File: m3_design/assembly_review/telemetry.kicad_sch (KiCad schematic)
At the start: 39 parts, among them J30 GNSS ANT SMA, J31 RADIO ANT SMA, Q30 AO3401A, Q31 AO3400A, Q32 S8550, U30 MAX-F10S-00B, U31 E22-900MM22S

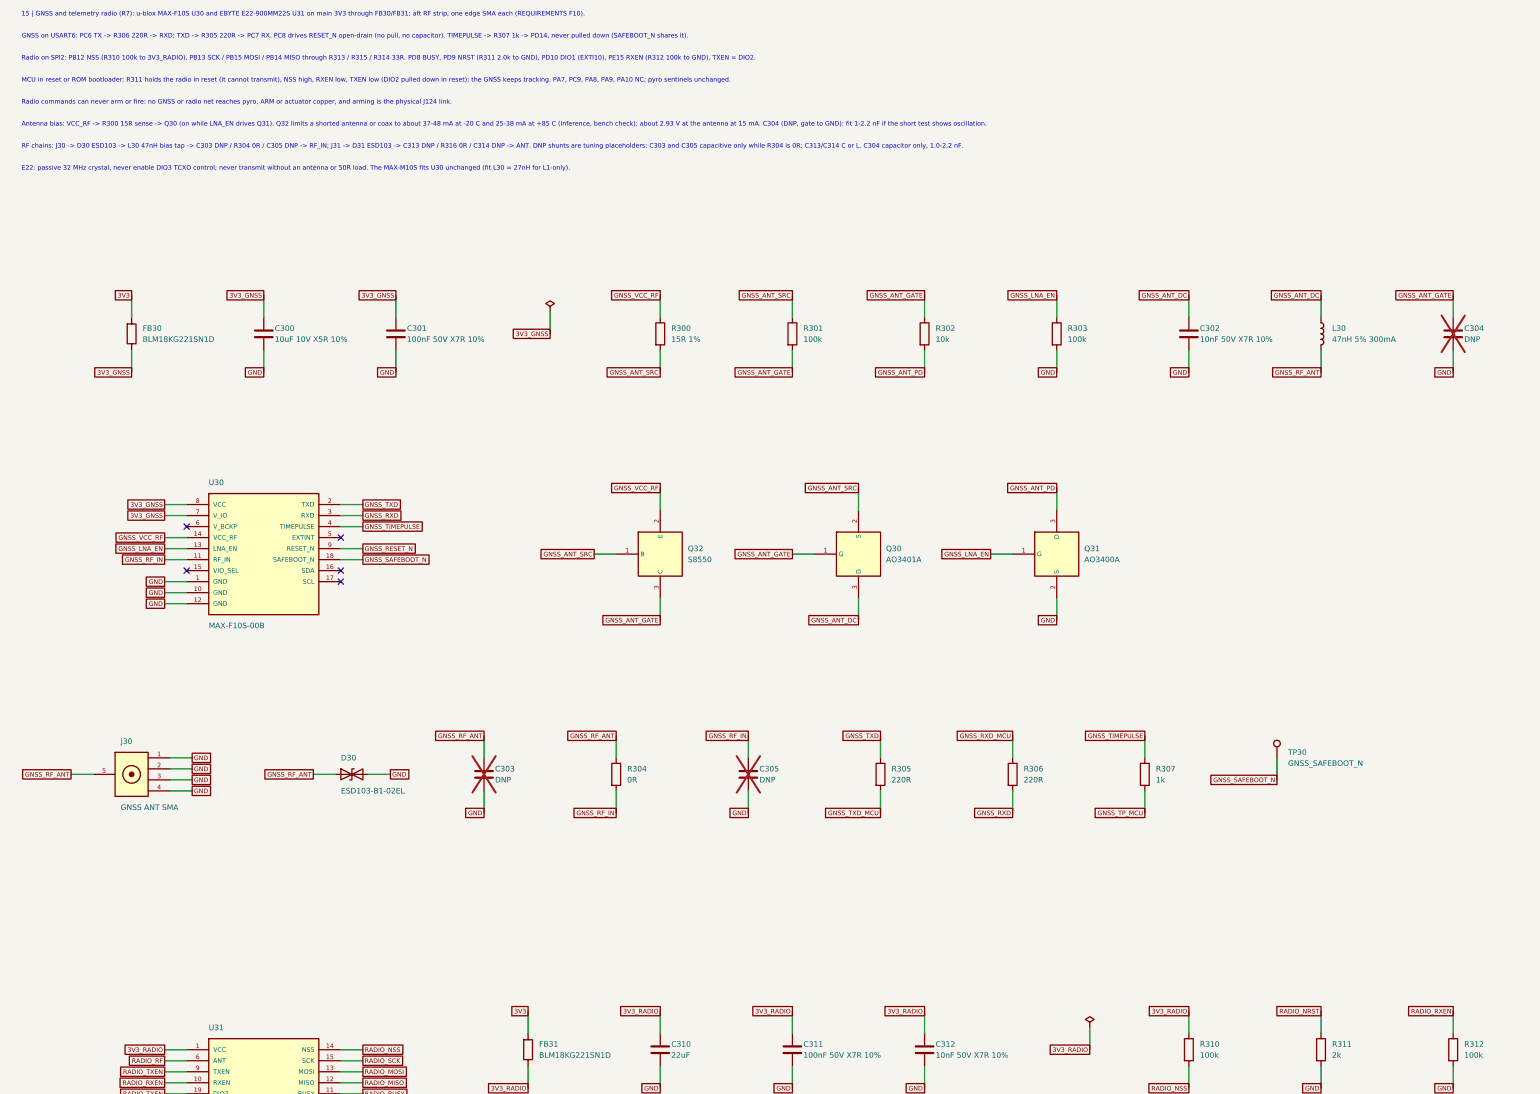
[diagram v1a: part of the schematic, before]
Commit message: M3-ASSY-R8: re-placed layout with planned-bus routing, owner-accepted deviations
R8 keeps R7's circuit, RF strip and CH1 pyro block (copied rigidly and
hash-asserted) and re-places everything else: U1 rotated so its free
pins face the RF strip, each block beside the U1 face it talks to, input
protection back at J1, and a fresh deterministic build (r8_build.sh)
with planned-bus routing, no autorouter and no patch stages.

Against R7: signal track 3.36 m -> 1.50 m, signal vias 217 -> 55,
simplicity index 100 -> 15.3, gate exceptions 74 -> 3, hard routing-rule
instances 10 -> 1, 7.7 A neck rise 38/30/44 -> 17.6/14.8/22.3 C,
unreferenced critical samples 27.9 % -> 11.1 %, non-pyro nets within
3 mm of armed copper 23 -> 7.

- Gate: check_r8 (pin contract from pin_table.tsv, F10 separation,
  battery/pyro clearance, loader-pin rule, rigid hashes), route_check
  profile r8, scorecard, dc_solve --necks, reference_audit, paste_check
- Review: passes 2, 3 and 4 found 0 Critical / 0 Major in all eight
  dimensions; pass 5 re-checked the final board (routing, planes,
  integrity) with 0 Critical / 0 Major
- Owner accepted the R8 deviation list on 2026-10-20, including the C10
  vibration item and the listed agent decisions

Board SHA-256 cc044ea0922ff826df19af9d9726d92c096ab2b127025b55d123d8772e5fb4a7.
tools/check.sh: DRC 0, unconnected 0, parity 0, ERC 0; audit, silk,
R8 contract, routing hygiene (0 failing, 3 allowlisted), actuator
contract and fit OK. Before ordering: consign U4, JLC tab acceptance,
cost/stock run within 24 h.

Co-Authored-By: Claude Opus 5.5 <noreply@anthropic.com>
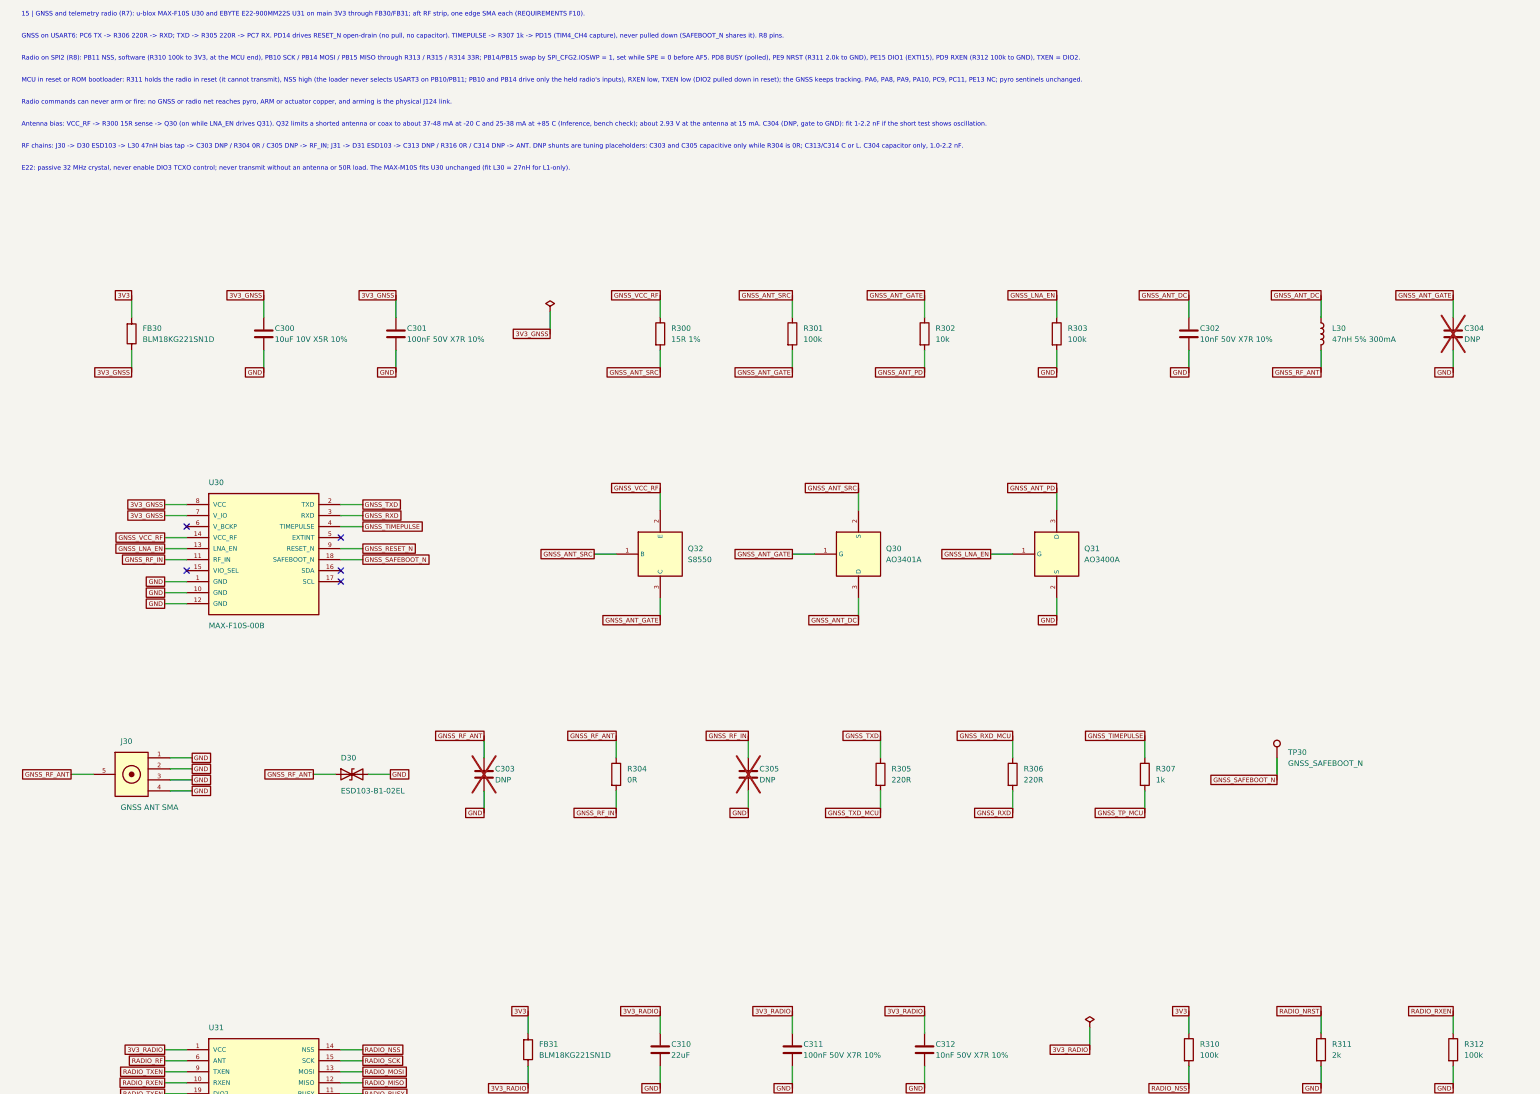
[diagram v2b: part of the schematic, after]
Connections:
- net 3V3: now also R310.1
- net 3V3_RADIO: no longer R310.1
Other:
- note added: "GNSS on USART6: PC6 TX -> R306 220R -> RXD; TXD -> R305 220R -> PC7 RX. PD14 drives RESET_N open-drain (no pull, no capacitor). TIMEPULSE -> R307 1k -> PD15 (TIM4_CH4 capture), never pulled down (SAFEBOOT_N shares it). R8 pins."
- note added: "MCU in reset or ROM bootloader: R311 holds the radio in reset (it cannot transmit), NSS high (the loader never selects USART3 on PB10/PB11; PB10 and PB14 drive only the held radio's inputs), RXEN low, TXEN low (DIO2 pulled down in reset); the GNSS keeps tracking. PA6, PA8, PA9, PA10, PC9, PC11, PE13 NC; pyro sentinels unchanged."
- note added: "Radio on SPI2 (R8): PB11 NSS, software (R310 100k to 3V3, at the MCU end), PB10 SCK / PB14 MOSI / PB15 MISO through R313 / R315 / R314 33R; PB14/PB15 swap by SPI_CFG2.IOSWP = 1, set while SPE = 0 before AF5. PD8 BUSY (polled), PE9 NRST (R311 2.0k to GND), PE15 DIO1 (EXTI15), PD9 RXEN (R312 100k to GND), TXEN = DIO2."
- note removed: "GNSS on USART6: PC6 TX -> R306 220R -> RXD; TXD -> R305 220R -> PC7 RX. PC8 drives RESET_N open-drain (no pull, no capacitor). TIMEPULSE -> R307 1k -> PD14, never pulled down (SAFEBOOT_N shares it)."
- note removed: "MCU in reset or ROM bootloader: R311 holds the radio in reset (it cannot transmit), NSS high, RXEN low, TXEN low (DIO2 pulled down in reset); the GNSS keeps tracking. PA7, PC9, PA8, PA9, PA10 NC; pyro sentinels unchanged."
- note removed: "Radio on SPI2: PB12 NSS (R310 100k to 3V3_RADIO), PB13 SCK / PB15 MOSI / PB14 MISO through R313 / R315 / R314 33R. PD8 BUSY, PD9 NRST (R311 2.0k to GND), PD10 DIO1 (EXTI10), PE15 RXEN (R312 100k to GND), TXEN = DIO2."
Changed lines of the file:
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@@
 		(title "15 | GNSS and telemetry radio (R7)")
 		(date "2026-10-15")
-		(rev "M3-ASSY-R7")
+		(rev "M3-ASSY-R8")
 		(company "Single-board M3 candidate; on-board GNSS and radio, not bench-verified"))
 	(text "15 | GNSS and telemetry radio (R7): u-blox MAX-F10S U30 and EBYTE E22-900MM22S U31 on main 3V3 through FB30/FB31; aft RF strip, one edge SMA each (REQUIREMENTS F10)."
@@
 			(justify left))
 )
-	(text "GNSS on USART6: PC6 TX -> R306 220R -> RXD; TXD -> R305 220R -> PC7 RX. PC8 drives RESET_N open-drain (no pull, no capacitor). TIMEPULSE -> R307 1k -> PD14, never pulled down (SAFEBOOT_N shares it)."
+	(text "GNSS on USART6: PC6 TX -> R306 220R -> RXD; TXD -> R305 220R -> PC7 RX. PD14 drives RESET_N open-drain (no pull, no capacitor). TIMEPULSE -> R307 1k -> PD15 (TIM4_CH4 capture), never pulled down (SAFEBOOT_N shares it). R8 pins."
 		(at 20.32 20.32 0)
 		(effects
@@
 			(justify left))
 )
-	(text "Radio on SPI2: PB12 NSS (R310 100k to 3V3_RADIO), PB13 SCK / PB15 MOSI / PB14 MISO through R313 / R315 / R314 33R. PD8 BUSY, PD9 NRST (R311 2.0k to GND), PD10 DIO1 (EXTI10), PE15 RXEN (R312 100k to GND), TXEN = DIO2."
+	(text "Radio on SPI2 (R8): PB11 NSS, software (R310 100k to 3V3, at the MCU end), PB10 SCK / PB14 MOSI / PB15 MISO through R313 / R315 / R314 33R; PB14/PB15 swap by SPI_CFG2.IOSWP = 1, set while SPE = 0 before AF5. PD8 BUSY (polled), PE9 NRST (R311 2.0k to GND), PE15 DIO1 (EXTI15), PD9 RXEN (R312 100k to GND), TXEN = DIO2."
 		(at 20.32 25.4 0)
 		(effects
@@
 			(justify left))
 )
-	(text "MCU in reset or ROM bootloader: R311 holds the radio in reset (it cannot transmit), NSS high, RXEN low, TXEN low (DIO2 pulled down in reset); the GNSS keeps tracking. PA7, PC9, PA8, PA9, PA10 NC; pyro sentinels unchanged."
+	(text "MCU in reset or ROM bootloader: R311 holds the radio in reset (it cannot transmit), NSS high (the loader never selects USART3 on PB10/PB11; PB10 and PB14 drive only the held radio's inputs), RXEN low, TXEN low (DIO2 pulled down in reset); the GNSS keeps tracking. PA6, PA8, PA9, PA10, PC9, PC11, PE13 NC; pyro sentinels unchanged."
 		(at 20.32 30.48 0)
 		(effects
@@
 			(type default))
 )
-	(global_label "3V3_RADIO"
+	(global_label "3V3"
 		(shape passive)
 		(at 289.56 245.11 0)

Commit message: R10: m3_design/r10_build.sh and per-family stage gate; m3_design/assembly_review rebuilt as M3-ASSY-R10 (board 883d2db5..., 46 x 90 mm); tools/check.sh passes at zero; binding note bound to the board
Co-Authored-By: Claude Opus 5.5 <noreply@anthropic.com>
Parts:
- removed C300: 10uF 10V X5R 10%, rocket:C0603, symbol M3:C
- removed C301, C311: 100nF 50V X7R 10%, rocket:C0402, symbol M3:C
- removed C302, C312: 10nF 50V X7R 10%, rocket:C0402, symbol M3:C
- removed C303, C304, C305, C313, C314: DNP, rocket:C0402_DNP, symbol M3:C
- removed C310: 22uF, rocket:C0805, symbol M3:C
- removed D30, D31: ESD103-B1-02EL, rocket:M3_TSLP_2_20, symbol M3:ESD_Bidir
- removed FB30, FB31: BLM18KG221SN1D, rocket:M3_BLM18K_0603, symbol M3:FerriteBead
- removed J30: GNSS ANT SMA, rocket:M3_SMA_KH_KE8_EDGE, symbol M3:SMA_Edge
- removed J31: RADIO ANT SMA, rocket:M3_SMA_KH_KE8_EDGE, symbol M3:SMA_Edge
- removed L30: 47nH 5% 300mA, rocket:M3_LQG15_0402, symbol M3:L
- removed Q30: AO3401A, rocket:SOT-23-3_L2.9-W1.3-P1.90-LS2.4-BR, symbol M3:PMOS_SOT23
- removed Q31: AO3400A, rocket:SOT-23-3_L2.9-W1.3-P1.90-LS2.4-BR, symbol M3:NMOS_SOT23
- removed Q32: S8550, rocket:SOT-23-3_L2.9-W1.3-P1.90-LS2.4-BR, symbol M3:PNP_SOT23
- removed R300: 15R 1%, rocket:R_0603_1608Metric, symbol M3:R
- removed R301, R303, R310, R312: 100k, rocket:R0402, symbol M3:R
- removed R302: 10k, rocket:R0402, symbol M3:R
- removed R304, R316: 0R, rocket:R0402, symbol M3:R
- removed R305, R306: 220R, rocket:R0402, symbol M3:R
- removed R307: 1k, rocket:R0402, symbol M3:R
- removed R311: 2k, rocket:R0402, symbol M3:R
- removed R313, R314, R315: 33R, rocket:R0402, symbol M3:R
- removed TP30: GNSS_SAFEBOOT_N, rocket:M3_TestPad_1.5, symbol M3:TestPoint
- removed U30: MAX-F10S-00B, rocket:M3_MAX_F10S_LCC18, symbol M3:MAX_F10S
- removed U31: E22-900MM22S, rocket:M3_E22_900MM22S, symbol M3:E22_900MM22S
- added C440, C443, C450, C453: 100nF 50V X7R 10%, rocket:C_0603_1608Metric, symbol M3:C
- added C441, C451: 1uF 50V X7R 10%, rocket:C_1206_3216Metric, symbol M3:C
- added C442, C452: 22uF 25V X7R 10%, rocket:M3_GRM32_1210, symbol M3:C
- added D410, D411, D420, D421: ESD103-B1-02EL, rocket:M3_TSLP_2_20, symbol M3:ESD_Bidir
- added J410: GPS 4V8/GND/TX/RX, rocket:M3_GH_BM04B_GHS_TBT, symbol M3:CameraTerminal
- added J420: RADIO 4V8/GND/TX/RX, rocket:M3_GH_BM04B_GHS_TBT, symbol M3:CameraTerminal
- added R440, R441, R443, R450, R451, R453: 1k 1%, rocket:R_0603_1608Metric, symbol M3:R
- added R442, R452: 10k 1%, rocket:R_0603_1608Metric, symbol M3:R
- added U411, U421: TXU0202DCUR, rocket:M3_TXU0202_DCU, symbol M3:CameraUART
- added U412, U422: TPS70933DBVR, rocket:M3_TPS709_DBV, symbol M3:CameraUARTSupply
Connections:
- net 3V3: now also C440.1, C450.1, U411.3 (VCCA MCU), U421.3 (VCCA MCU)
- net GND: now also C440.2, C441.2, C442.2, C443.2, C450.2, C451.2, C452.2, C453.2, D410.2 (A2), D411.2 (A2), D420.2 (A2), D421.2 (A2), J410.2 (GND), J420.2 (GND), R442.2, R443.2, R452.2, R453.2, U411.2 (GND), U412.2 (GND), U421.2 (GND), U422.2 (GND)
- new net GPS_4V8: C441.1, J410.1 (5V OUT), U412.1 (IN)
- new net GPS_IO_3V3: C442.1, C443.1, R443.1, U411.7 (VCCB CAMERA), U412.5 (OUT3.3V)
- new net GPS_RX_BUFFER: R440.2, U411.1 (B2 FROM CAMERA)
- new net GPS_RX_MCU: U411.4 (A2Y RX OUTPUT)
- new net GPS_RX_WIRE: D411.1 (A1), J410.4 (TX TO CAMERA RX), R440.1
- new net GPS_TX_BUFFER: R441.1, U411.8 (B1Y TO CAMERA)
- new net GPS_TX_MCU: U411.5 (A1 TX INPUT)
- new net GPS_TX_WIRE: D410.1 (A1), J410.3 (RX FROM CAMERA TX), R441.2
- new net GPS_UART_OE: R442.1, U411.6 (OE)
- new net RADIO_4V8: C451.1, J420.1 (5V OUT), U422.1 (IN)
- new net RADIO_IO_3V3: C452.1, C453.1, R453.1, U421.7 (VCCB CAMERA), U422.5 (OUT3.3V)
- new net RADIO_RX_BUFFER: R450.2, U421.1 (B2 FROM CAMERA)
- new net RADIO_RX_MCU: U421.4 (A2Y RX OUTPUT)
- new net RADIO_RX_WIRE: D421.1 (A1), J420.4 (TX TO CAMERA RX), R450.1
- new net RADIO_TX_BUFFER: R451.1, U421.8 (B1Y TO CAMERA)
- new net RADIO_TX_MCU: U421.5 (A1 TX INPUT)
- new net RADIO_TX_WIRE: D420.1 (A1), J420.3 (RX FROM CAMERA TX), R451.2
- new net RADIO_UART_OE: R452.1, U421.6 (OE)
- no-connect marks 10 -> 4
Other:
- note added: "GPS USART6 PC6 TX / PC7 RX AF7; radio UART5 PB13 TX / PB12 RX AF14 (DS12110 Rev10 Table11 p90)."
- note added: "R10: external GPS J410 and radio J420. GH4 pins 1 supply, 2 GND, 3 board TX, 4 board RX; harness crosses TX to endpoint RX."
- note added: "Radio USB-powered with board off: TXU partial-power-down isolation protects MCU; power-pin reverse/transient qualification remains a separate bench gate."
- note added: "Radio messages may never arm/fire; no port signal reaches pyro, arming or actuator nets. Configure LR900 channels within 902-928MHz."
- note added: "Reset / boot / off: EN=0 and OE=0. Startup: EN, stable downstream supply, UART idle-high configuration, then OE. Shutdown: OE low before EN low."
- note added: "TXU0202 VCCA = main 3V3, VCCB = own switched TPS70933 output. OE has 10k pull-down. 1k UART series resistors and ground-only ESD clamps."
- note removed: "15 | GNSS and telemetry radio (R7): u-blox MAX-F10S U30 and EBYTE E22-900MM22S U31 on main 3V3 through FB30/FB31; aft RF strip, one edge SMA each (REQUIREMENTS F10)."
- note removed: "Antenna bias: VCC_RF -> R300 15R sense -> Q30 (on while LNA_EN drives Q31). Q32 limits a shorted antenna or coax to about 37-48 mA at -20 C and 25-38 mA at +85 C (Inference, bench check); about 2.93 V at the antenna at 15 mA. C304 (DNP, gate to GND): fit 1-2.2 nF if the short test shows oscillation."
- note removed: "E22: passive 32 MHz crystal, never enable DIO3 TCXO control; never transmit without an antenna or 50R load. The MAX-M10S fits U30 unchanged (fit L30 = 27nH for L1-only)."
- note removed: "GNSS on USART6: PC6 TX -> R306 220R -> RXD; TXD -> R305 220R -> PC7 RX. PD14 drives RESET_N open-drain (no pull, no capacitor). TIMEPULSE -> R307 1k -> PD15 (TIM4_CH4 capture), never pulled down (SAFEBOOT_N shares it). R8 pins."
- note removed: "MCU in reset or ROM bootloader: R311 holds the radio in reset (it cannot transmit), NSS high (the loader never selects USART3 on PB10/PB11; PB10 and PB14 drive only the held radio's inputs), RXEN low, TXEN low (DIO2 pulled down in reset); the GNSS keeps tracking. PA6, PA8, PA9, PA10, PC9, PC11, PE13 NC; pyro sentinels unchanged."
- note removed: "RF chains: J30 -> D30 ESD103 -> L30 47nH bias tap -> C303 DNP / R304 0R / C305 DNP -> RF_IN; J31 -> D31 ESD103 -> C313 DNP / R316 0R / C314 DNP -> ANT. DNP shunts are tuning placeholders: C303 and C305 capacitive only while R304 is 0R; C313/C314 C or L. C304 capacitor only, 1.0-2.2 nF."
- note removed: "Radio commands can never arm or fire: no GNSS or radio net reaches pyro, ARM or actuator copper, and arming is the physical J124 link."
- note removed: "Radio on SPI2 (R8): PB11 NSS, software (R310 100k to 3V3, at the MCU end), PB10 SCK / PB14 MOSI / PB15 MISO through R313 / R315 / R314 33R; PB14/PB15 swap by SPI_CFG2.IOSWP = 1, set while SPE = 0 before AF5. PD8 BUSY (polled), PE9 NRST (R311 2.0k to GND), PE15 DIO1 (EXTI15), PD9 RXEN (R312 100k to GND), TXEN = DIO2."
- company: Single-board M3 candidate; on-board GNSS and radio, not bench-verified -> (none)
- title: 15 | GNSS and telemetry radio (R7) -> 15 | External GPS and radio UART ports
